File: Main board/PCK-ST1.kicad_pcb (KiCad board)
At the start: 4 copper layers, 68.5 x 55.6 mm, 166 parts, among them IC1 DRV8426RGER, IC2 DRV8426RGER, IC3 DRV8426RGER, IC4 DRV8426RGER, IC5 TLV70033DDCR, IC7 TPS2121RUXR, IC8 TPS25730DREFR, J1 Conn_02x20_Odd_Even, J10 RA, J11 EL, J12 AZ, J13 GPS, J14 SHUTTER, J15 PWR_ON, J16 BOOT, J17 Conn_01x02, J2 RJE05-166-1310, J3 Conn_01x04, J4 Conn_01x04, J5 Conn_01x04, J6 Conn_01x04, J7 USB_C_Receptacle_USB2.0_16P, J8 Barrel_Jack_Switch_Pin3Ring, J9 DEC, Q1 2N7002, U1 STM32L476RGTx, U2 TLP293, U3 TLP293, Y1 16MHz/10pF

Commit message: updt
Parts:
- added C53: 100n, Capacitor_SMD:C_0402_1005Metric, F.Cu at (155.3, 100.4)
- added R59: 100k, Resistor_SMD:R_0402_1005Metric, F.Cu at (152.5, 98.2)
- added R60: 100k, Resistor_SMD:R_0402_1005Metric, F.Cu at (152.4, 100.4)
- R43, R44: value 2k -> 2k2
- moved D4 0.33 mm to (129.8, 68.9)
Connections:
- R34 pad 1: GND -> +3V3
- R35 pad 1: GND -> +3V3
- R36 pad 1: GND -> +3V3
- R37 pad 1: GND -> +3V3
- U1 pad 11: unconnected-(U1-PC3-Pad11) -> /MCU/VIN_ADC
- U1 pad 56: /MCU/USB_LED -> /MCU/DC_LED
- U1 pad 57: /MCU/DC_LED -> /MCU/USB_LED
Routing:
- net /MCU/VIN_ADC: track 0.00 -> 20.8 mm, vias 0 -> 2
- net +12V: track 47.7 -> 42.1 mm
- net +3V3: track 24.8 -> 28.8 mm, vias 18 -> 22
- net /MCU/DC_LED: track 15.2 -> 11.3 mm
- net /MCU/USB_LED: track 15.4 -> 13.0 mm
- net GND: track 66.9 -> 66.8 mm, vias 195 -> 203
- added copper zone on In2.Cu, net GND
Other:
- board text added: "PCK Tech"

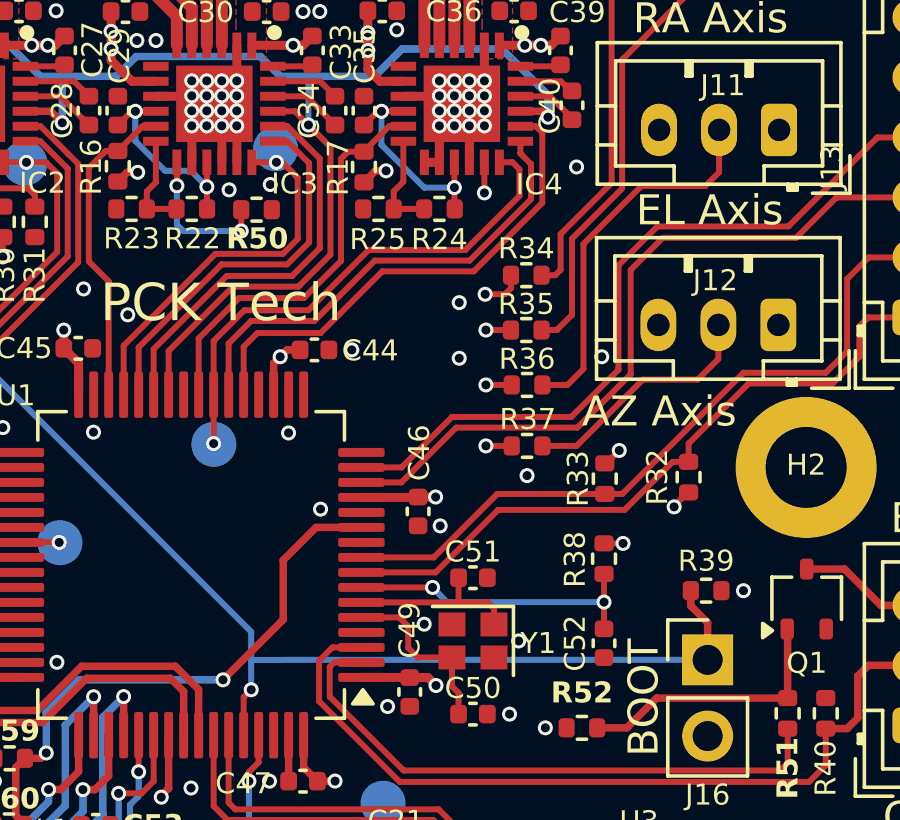
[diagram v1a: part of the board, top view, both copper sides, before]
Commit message: Updated endstops routing
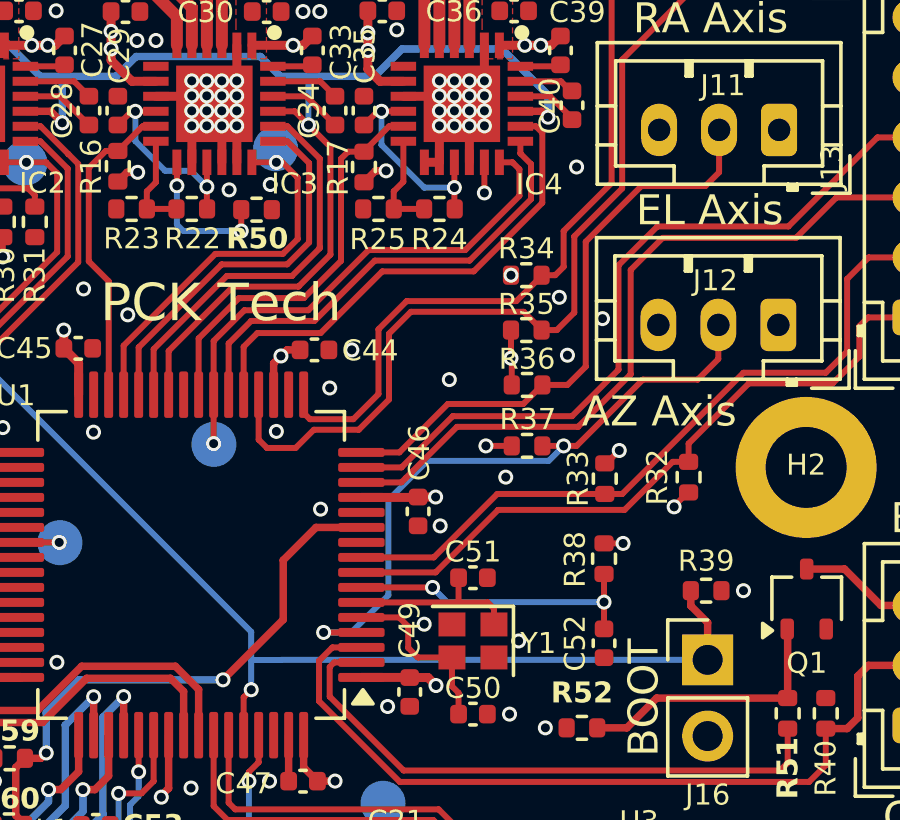
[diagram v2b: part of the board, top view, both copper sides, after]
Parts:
- R60: value 100k -> 22k
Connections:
- U1 pad 16: unconnected-(U1-PA2-Pad16) -> /MCU/EL_LIM
- U1 pad 17: unconnected-(U1-PA3-Pad17) -> /MCU/DEC_LIM
- U1 pad 20: unconnected-(U1-PA4-Pad20) -> /MCU/RA_LIM
- U1 pad 4: unconnected-(U1-PC15-Pad4) -> /MCU/AZ_LIM
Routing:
- net /MCU/RA_LIM: track 15.9 -> 30.4 mm
- net /MCU/AZ_LIM: track 8.20 -> 21.9 mm, vias 0 -> 2
- net /MCU/DEC_LIM: track 20.6 -> 32.5 mm
- net /MCU/EL_LIM: track 12.7 -> 19.6 mm
- net +3V3: track 28.8 -> 27.6 mm, vias 22 -> 21
- net GND: vias 203 -> 205

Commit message: Updated layout v0.2
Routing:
- net GND: vias 205 -> 207
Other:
- board text added: "Main board"
- board text removed: "PCK Tech"

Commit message: As built updated
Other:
- board text added: "GND 12V"
- board text removed: "12V GND"
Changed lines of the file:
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@@
 		)
 	)
-	(gr_text "12V\n\nGND"
+	(gr_text "GND\n\n12V"
 		(at 185.9026 67.7926 0)
 		(layer "B.SilkS")

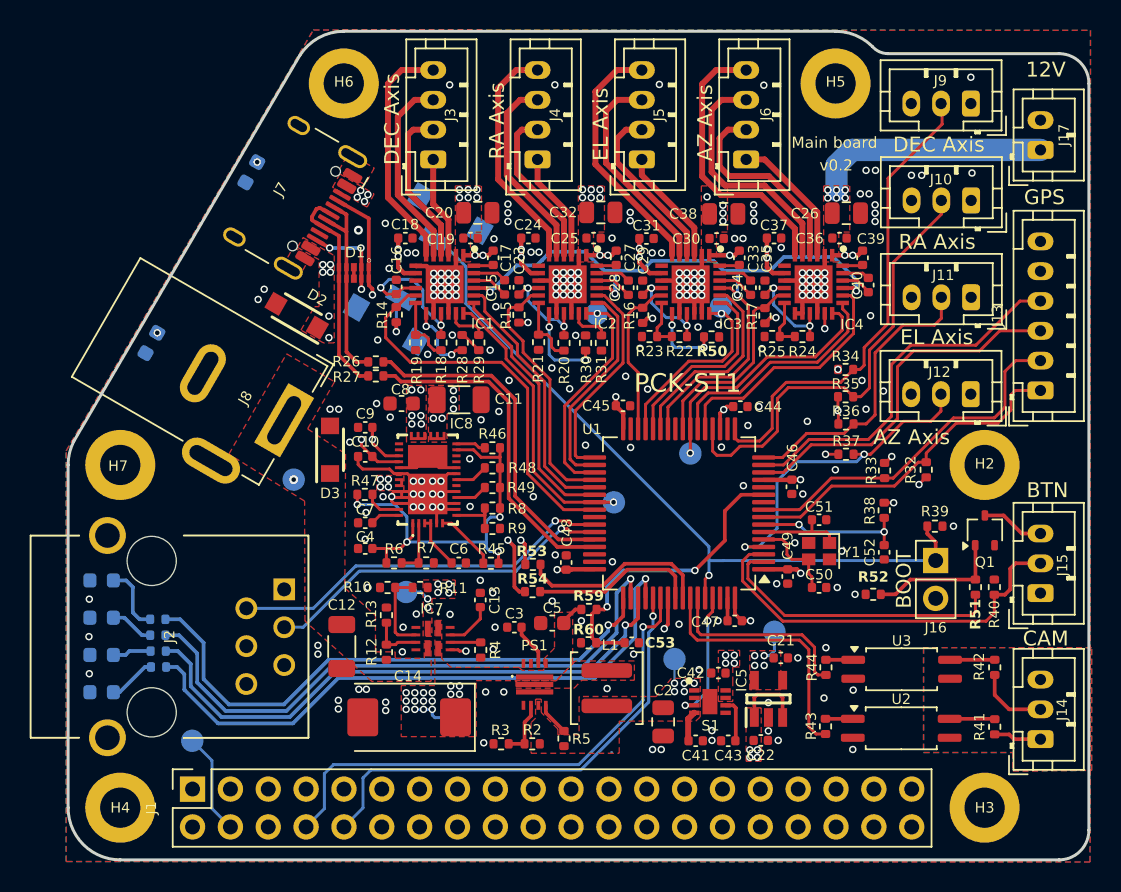
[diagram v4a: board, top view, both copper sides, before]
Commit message: Main board updated to v0.3
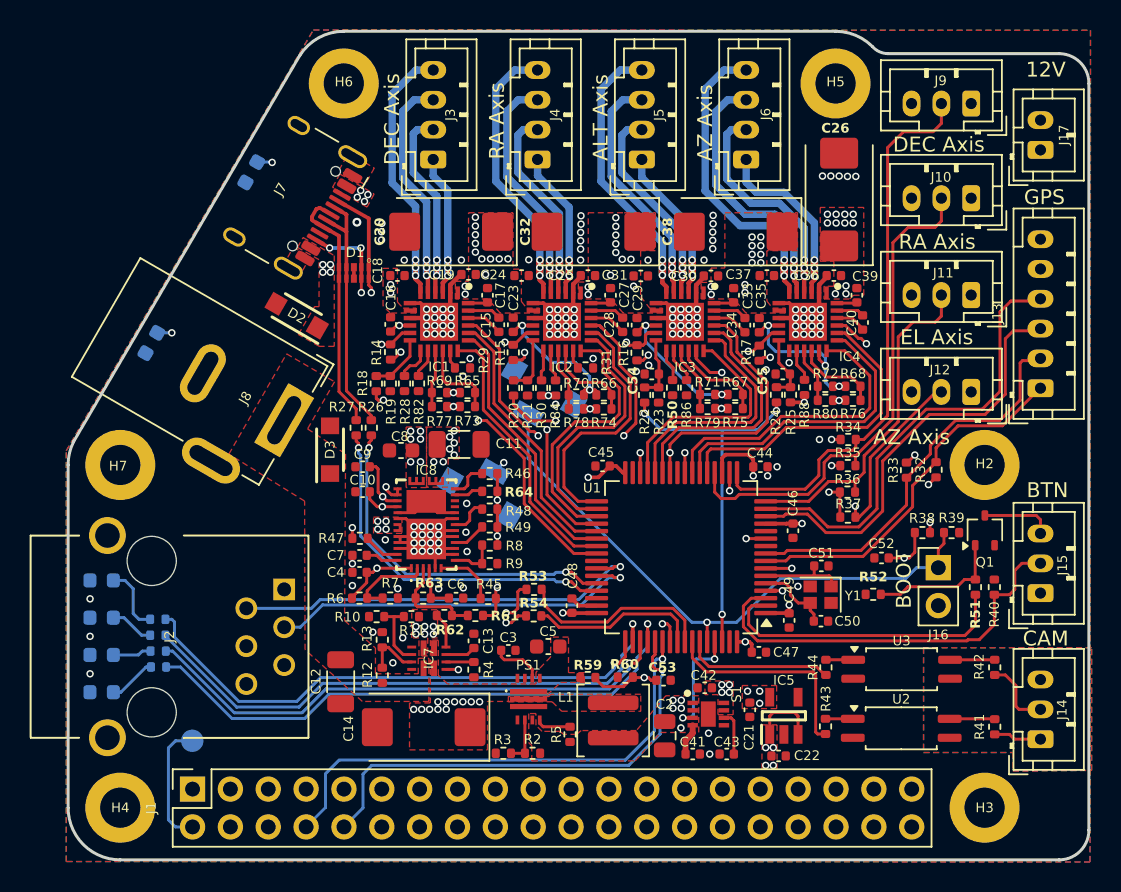
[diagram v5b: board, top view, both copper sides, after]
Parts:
- removed S2: TL3336AF160Q, SamacSys_Parts.pretty:TL3336AF160Q
- removed TP1, TP10, TP2, TP3, TP5, TP6, TP7, TP8, TP9: TestPoint, TestPoint:TestPoint_Pad_D1.5mm
- added C54: 100n, Capacitor_SMD:C_0402_1005Metric, F.Cu at (156.7, 82.4)
- added C55: 100n, Capacitor_SMD:C_0402_1005Metric, F.Cu at (165.5, 82.4)
- added R61: 200k, Resistor_SMD:R_0402_1005Metric, F.Cu at (144.8, 98.6)
- added R62: 24k, Resistor_SMD:R_0402_1005Metric, F.Cu at (142.7, 98.6)
- added R63: 0R, Resistor_SMD:R_0402_1005Metric, F.Cu at (141.3, 97.4)
- added R64: 100k, Resistor_SMD:R_0402_1005Metric, F.Cu at (145.8, 90.3)
- added R65: 0R, Resistor_SMD:R_0402_1005Metric, F.Cu at (144.3, 83.6)
- added R66: 0R, Resistor_SMD:R_0402_1005Metric, F.Cu at (153.5, 83.8)
- added R67: 0R, Resistor_SMD:R_0402_1005Metric, F.Cu at (162.3, 83.8)
- added R68: 0R, Resistor_SMD:R_0402_1005Metric, F.Cu at (170.2, 83.2)
- added R69: 0R, Resistor_SMD:R_0402_1005Metric, F.Cu at (142.4, 83.6)
- added R70: 0R, Resistor_SMD:R_0402_1005Metric, F.Cu at (151.6, 83.8)
- added R71: 0R, Resistor_SMD:R_0402_1005Metric, F.Cu at (160.4, 83.8)
- added R72: 0R, Resistor_SMD:R_0402_1005Metric, F.Cu at (168.3, 83.2)
- added R73: 0R, Resistor_SMD:R_0402_1005Metric, F.Cu at (144.3, 84.6)
- added R74: 0R, Resistor_SMD:R_0402_1005Metric, F.Cu at (153.5, 84.7)
- added R75: 0R, Resistor_SMD:R_0402_1005Metric, F.Cu at (162.3, 84.7)
- added R76: 0R, Resistor_SMD:R_0402_1005Metric, F.Cu at (170.2, 84.2)
- added R77: 0R, Resistor_SMD:R_0402_1005Metric, F.Cu at (142.4, 84.6)
- added R78: 0R, Resistor_SMD:R_0402_1005Metric, F.Cu at (151.6, 84.7)
- added R79: 0R, Resistor_SMD:R_0402_1005Metric, F.Cu at (160.4, 84.7)
- added R80: 0R, Resistor_SMD:R_0402_1005Metric, F.Cu at (168.3, 84.2)
- added R82: 0R, Resistor_SMD:R_0402_1005Metric, F.Cu at (141.0, 83.0)
- added R84: 0R, Resistor_SMD:R_0402_1005Metric, F.Cu at (150.2, 83.3)
- added R86: 0R, Resistor_SMD:R_0402_1005Metric, F.Cu at (159.0, 83.3)
- added R88: 0R, Resistor_SMD:R_0402_1005Metric, F.Cu at (166.9, 83.3)
- added SW1: SW_Push, SamacSys_Parts.pretty:TL3336AF160Q, B.Cu at (144.2, 85.2)
- C14: value 47u/25V -> 100u/20V
- C20, C26, C32, C38: value 22uF/16V -> 100u/20V; footprint Capacitor_SMD:C_0805_2012Metric -> Capacitor_Tantalum_SMD:CP_EIA-7343-15_Kemet-W
- IC1, IC2, IC3, IC4: value DRV8426RGER -> DRV8434
- R11, R12: value 71k5 -> 75k
- moved R18 5.14 mm to (138.2, 83.0), turned to -90 degrees
- moved R28 4.74 mm to (140.1, 83.0), turned to -90 degrees
- moved R34 4.70 mm to (169.8, 86.8)
- moved R35 4.63 mm to (169.8, 88.5)
- moved R36 4.57 mm to (169.8, 90.3)
- moved R59 4.57 mm to (152.4, 102.8)
- moved R22 4.56 mm to (156.2, 83.8), turned to -90 degrees
- moved R20 4.53 mm to (147.4, 83.3), turned to -90 degrees
- moved R26 4.43 mm to (137.8, 86.0), turned to -90 degrees
- moved R50 4.30 mm to (158.1, 83.3), turned to 90 degrees
- moved R24 4.28 mm to (165.0, 83.8), turned to -90 degrees
- moved C45 4.27 mm to (153.4, 88.6), turned to 180 degrees
- moved C44 4.26 mm to (164.0, 88.6)
- moved R30 4.22 mm to (149.3, 83.3), turned to -90 degrees
- moved R37 4.22 mm to (169.8, 92.0)
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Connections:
- net /EL Stepper driver/DIR renamed /ALT Stepper driver/DIR
- net /EL Stepper driver/ENABLE renamed /ALT Stepper driver/ENABLE
- net /EL Stepper driver/M0 renamed /ALT Stepper driver/M0
- net /EL Stepper driver/STEP renamed /ALT Stepper driver/STEP
- net /EL Stepper driver/VREF renamed /ALT Stepper driver/VREF
- net /EL Stepper driver/nFAULT renamed /ALT Stepper driver/nFAULT
- net /Power/CC1 renamed /Power_Delivery/CC1
- net /Power/CC2 renamed /Power_Delivery/CC2
- net /Power/VBUS renamed /Power_Delivery/VBUS
- net /Power/VIN_3V3 renamed /Power_Delivery/VIN_3V3
- net Net-(IC8-ADCIN1) renamed /Power_Delivery/ADC1
- net Net-(IC8-ADCIN4) renamed /Power_Delivery/ADC4
- C29 pad 1: /EL Stepper driver/DVDD -> /ALT Stepper driver/DVDD
- C4 pad 1: /Power/LDO_3V3 -> /Power_Delivery/LDO_3V3
- C6 pad 1: /Power/LDO_1V5 -> /Power_Delivery/LDO_1V5
- IC1 pad 14: GND -> Net-(IC1-TOFF)
- IC1 pad 15: /DEC Stepper driver/DVDD -> Net-(IC1-DECAY1)
- IC1 pad 16: GND -> Net-(IC1-DECAY0)
- IC2 pad 14: GND -> Net-(IC2-TOFF)
- IC2 pad 15: /RA Stepper driver/DVDD -> Net-(IC2-DECAY1)
- IC2 pad 16: GND -> Net-(IC2-DECAY0)
- IC3 pad 10: /EL Stepper driver/DVDD -> /ALT Stepper driver/DVDD
- IC3 pad 14: GND -> Net-(IC3-TOFF)
- IC3 pad 15: /EL Stepper driver/DVDD -> Net-(IC3-DECAY1)
- IC3 pad 16: GND -> Net-(IC3-DECAY0)
- IC4 pad 14: GND -> Net-(IC4-TOFF)
- IC4 pad 15: /AZ Stepper driver/DVDD -> Net-(IC4-DECAY1)
- IC4 pad 16: GND -> Net-(IC4-DECAY0)
- IC4 pad 17: +3V3 -> /AZ Stepper driver/DVDD
- IC8 pad 1: /Power/LDO_3V3 -> /Power_Delivery/LDO_3V3
- IC8 pad 18: /Power/LDO_3V3 -> Net-(IC8-~{FAULT_IN})
- IC8 pad 3: /Power/LDO_1V5 -> /Power_Delivery/ADC2
- IC8 pad 4: /Power/LDO_1V5 -> /Power_Delivery/LDO_1V5
- R22 pad 2: /EL Stepper driver/DVDD -> /MCU/IREG
- R24 pad 2: /AZ Stepper driver/DVDD -> /MCU/IREG
- R45 pad 2: /Power/LDO_3V3 -> /Power_Delivery/LDO_3V3
- R46 pad 2: /Power/LDO_3V3 -> /Power_Delivery/LDO_3V3
- R47 pad 2: /Power/LDO_3V3 -> /Power_Delivery/LDO_3V3
- R48 pad 1: Net-(IC8-PLUG_FLIP) -> /Power_Delivery/LDO_3V3
- R48 pad 2: /Power/LDO_3V3 -> Net-(IC8-PLUG_FLIP)
- R49 pad 1: Net-(IC8-DBG_ACC) -> /Power_Delivery/LDO_3V3
- R49 pad 2: /Power/LDO_3V3 -> Net-(IC8-DBG_ACC)
- R6 pad 2: /Power/LDO_3V3 -> /Power_Delivery/LDO_3V3
- R8 pad 2: /Power/LDO_3V3 -> /Power_Delivery/LDO_3V3
- U1 pad 62: unconnected-(U1-PB9-Pad62) -> /MCU/IREG
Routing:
- net /Power_Delivery/LDO_3V3: track 0.00 -> 31.7 mm, vias 0 -> 5
- net /Power/LDO_3V3: track 28.6 -> 0.00 mm, vias 4 -> 0
- net +12V: track 42.1 -> 14.9 mm, vias 53 -> 59
- net /MCU/IREG: track 0.00 -> 25.5 mm, vias 0 -> 3
- net /STEP_n_SLEEP: track 49.5 -> 70.6 mm
- net /RA Stepper driver/DVDD: track 6.95 -> 17.7 mm, vias 2 -> 3
- net /ALT Stepper driver/DVDD: track 0.00 -> 9.96 mm, vias 0 -> 2
- net /MCU/BOOT: track 49.7 -> 40.4 mm
- net /DEC Stepper driver/DVDD: track 10.5 -> 18.0 mm, vias 2 -> 3
- net /EL Stepper driver/DVDD: track 7.02 -> 0.00 mm, vias 2 -> 0
- net /Power_Delivery/ADC2: track 0.00 -> 6.74 mm
- net Net-(IC3-DECAY0): track 0.00 -> 6.30 mm
- net Net-(IC2-DECAY0): track 0.00 -> 6.08 mm
- net /Power_Delivery/CC2: track 19.4 -> 25.2 mm
- net Net-(IC4-DECAY0): track 0.00 -> 5.69 mm
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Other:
- board text added: "ALT Axis"
- board text added: "PCK-ST1 Main Board"
- board text added: "by JOSEF PECKA"
- board text added: "version 0.3 2025-12-02"
- board text removed: "Main board"
- board text removed: "PCK-ST1"
- board text removed: "v0.2"
